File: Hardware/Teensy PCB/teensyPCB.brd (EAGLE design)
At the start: 100 x 50 mm, 4 parts, among them U1 HC_05

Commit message: updates
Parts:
- added TOBALANCE: (no value), SparkFun-Connectors:MOLEX-1X6_LOCK
- added U2: USD-SOCKETNEW, SparkFun-Connectors:MICRO-SD-SOCKET-PP
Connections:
- new net 5V: TOBALANCE.6
- new net ARDUINO_RX: TOBALANCE.3
- new net ARDUINO_TX: TOBALANCE.2
- new net ENABLE: TOBALANCE.1
- net 3.3V: now also TOBALANCE.5
- net GND: now also TOBALANCE.4; no longer U$1.10, U$1.11, U$1.12, U$1.13, U$1.14/A0, U$1.15/A1, U$1.18/A4, U$1.19/A5, U$1.22/A8, U$1.23/A9, U$1.7, U$1.9
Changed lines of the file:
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@@
 <layer number="54" name="bGND_GNDA" color="1" fill="9" visible="no" active="no"/>
 <layer number="56" name="wert" color="7" fill="1" visible="yes" active="yes"/>
+<layer number="57" name="tCAD" color="7" fill="1" visible="no" active="no"/>
 <layer number="90" name="Modules" color="5" fill="1" visible="no" active="no"/>
 <layer number="91" name="Nets" color="2" fill="1" visible="no" active="no"/>
@@
 <layer number="97" name="Info" color="7" fill="1" visible="no" active="no"/>
 <layer number="98" name="Guide" color="6" fill="1" visible="no" active="no"/>
+<layer number="99" name="SpiceOrder" color="7" fill="1" visible="no" active="no"/>
 <layer number="100" name="Muster" color="7" fill="1" visible="no" active="no"/>
 <layer number="101" name="Patch_Top" color="12" fill="4" visible="yes" active="yes"/>
@@
 <layer number="108" name="tplace-old" color="10" fill="1" visible="no" active="yes"/>
 <layer number="109" name="ref-old" color="11" fill="1" visible="no" active="yes"/>
+<layer number="110" name="fp0" color="7" fill="1" visible="yes" active="yes"/>
+<layer number="111" name="LPC17xx" color="7" fill="1" visible="yes" active="yes"/>
+<layer number="112" name="tSilk" color="7" fill="1" visible="yes" active="yes"/>
+<layer number="113" name="IDFDebug" color="4" fill="1" visible="yes" active="yes"/>
 <layer number="116" name="Patch_BOT" color="9" fill="4" visible="yes" active="yes"/>
 <layer number="121" name="_tsilk" color="7" fill="1" visible="yes" active="yes"/>
 <layer number="122" name="_bsilk" color="7" fill="1" visible="yes" active="yes"/>
+<layer number="123" name="tTestmark" color="7" fill="1" visible="yes" active="yes"/>
+<layer number="124" name="bTestmark" color="7" fill="1" visible="yes" active="yes"/>
 <layer number="125" name="_tNames" color="7" fill="1" visible="yes" active="yes"/>
+<layer number="126" name="_bNames" color="7" fill="1" visible="yes" active="yes"/>
+<layer number="127" name="_tValues" color="7" fill="1" visible="yes" active="yes"/>
+<layer number="128" name="_bValues" color="7" fill="1" visible="yes" active="yes"/>
+<layer number="131" name="tAdjust" color="7" fill="1" visible="yes" active="yes"/>
+<layer number="132" name="bAdjust" color="7" fill="1" visible="yes" active="yes"/>
 <layer number="144" name="Drill_legend" color="7" fill="1" visible="yes" active="yes"/>
+<layer number="150" name="Notes" color="7" fill="1" visible="yes" active="yes"/>
 <layer number="151" name="HeatSink" color="7" fill="1" visible="yes" active="yes"/>
+<layer number="152" name="_bDocu" color="7" fill="1" visible="yes" active="yes"/>
+<layer number="153" name="FabDoc1" color="7" fill="1" visible="yes" active="yes"/>
+<layer number="154" name="FabDoc2" color="7" fill="1" visible="yes" active="yes"/>
+<layer number="155" name="FabDoc3" color="7" fill="1" visible="yes" active="yes"/>
 <layer number="199" name="Contour" color="7" fill="1" visible="yes" active="yes"/>
 <layer number="200" name="200bmp" color="1" fill="10" visible="no" active="no"/>
@@
 <layer number="223" name="223bmp" color="24" fill="1" visible="no" active="no"/>
 <layer number="224" name="224bmp" color="25" fill="1" visible="no" active="no"/>
+<layer number="248" name="Housing" color="7" fill="1" visible="yes" active="yes"/>
+<layer number="249" name="Edge" color="7" fill="1" visible="yes" active="yes"/>
 <layer number="250" name="Descript" color="3" fill="1" visible="no" active="no"/>
 <layer number="251" name="SMDround" color="12" fill="11" visible="no" active="no"/>
@@
 <element name="J_BT_BOARD_1" library="Bluetooth_HC-05" package="BT_BOARD_FOOTPRINT" value="BLUETOOTH_BOARD" x="85" y="35"/>
 <element name="J_ULTRASONIC_1" library="HC-SR04" package="HC-SR04_FOOTPRINT" value="HC-SR04" x="10" y="35"/>
+<element name="U2" library="SparkFun-Connectors" package="MICRO-SD-SOCKET-PP" value="USD-SOCKETNEW" x="-60" y="5"/>
+<element name="TOBALANCE" library="SparkFun-Connectors" package="MOLEX-1X6_LOCK" value="" x="-70" y="-5"/>
 </elements>
 <signals>
@@
 <contactref element="U$1" pad="GND"/>
 <contactref element="U$1" pad="GND2"/>
-<contactref element="U$1" pad="18/A4"/>
-<contactref element="U$1" pad="19/A5"/>
-<contactref element="U$1" pad="11"/>
-<contactref element="U$1" pad="9"/>
-<contactref element="U$1" pad="23/A9"/>
-<contactref element="U$1" pad="22/A8"/>
-<contactref element="U$1" pad="13"/>
-<contactref element="U$1" pad="15/A1"/>
-<contactref element="U$1" pad="12"/>
-<contactref element="U$1" pad="14/A0"/>
-<contactref element="U$1" pad="7"/>
-<contactref element="U$1" pad="10"/>
-<wire x1="62.62" y1="31.35" x2="62.62" y2="33.89" width="0" layer="19" extent="1-1"/>
-<wire x1="62.62" y1="23.73" x2="62.62" y2="31.35" width="0" layer="19" extent="1-1"/>
-<wire x1="62.62" y1="21.19" x2="62.62" y2="23.73" width="0" layer="19" extent="1-1"/>
-<wire x1="55" y1="23.73" x2="62.62" y2="23.73" width="0" layer="19" extent="1-1"/>
-<wire x1="62.62" y1="13.57" x2="62.62" y2="21.19" width="0" layer="19" extent="1-1"/>
-<wire x1="62.62" y1="11.03" x2="62.62" y2="13.57" width="0" layer="19" extent="1-1"/>
-<wire x1="62.62" y1="8.49" x2="62.62" y2="11.03" width="0" layer="19" extent="1-1"/>
-<wire x1="55" y1="8.49" x2="62.62" y2="8.49" width="0" layer="19" extent="1-1"/>
-<wire x1="47.38" y1="8.49" x2="55" y2="8.49" width="0" layer="19" extent="1-1"/>
-<wire x1="47.38" y1="11.03" x2="47.38" y2="8.49" width="0" layer="19" extent="1-1"/>
-<wire x1="47.38" y1="13.57" x2="47.38" y2="11.03" width="0" layer="19" extent="1-1"/>
-<wire x1="47.38" y1="16.11" x2="47.38" y2="13.57" width="0" layer="19" extent="1-1"/>
-<wire x1="47.38" y1="21.19" x2="47.38" y2="16.11" width="0" layer="19" extent="1-1"/>
-<wire x1="47.38" y1="41.51" x2="62.62" y2="33.89" width="0" layer="19" extent="1-1"/>
+<contactref element="TOBALANCE" pad="4"/>
+<wire x1="55" y1="23.73" x2="47.38" y2="41.51" width="0" layer="19" extent="1-1"/>
+<wire x1="55" y1="8.49" x2="55" y2="23.73" width="0" layer="19" extent="1-1"/>
+<wire x1="-62.38" y1="-5.254" x2="55" y2="8.49" width="0" layer="19" extent="1-1"/>
 </signal>
 <signal name="VIN">
@@
 <contactref element="U$1" pad="3.3V1"/>
 <contactref element="U$1" pad="3.3V"/>
+<contactref element="TOBALANCE" pad="5"/>
 <wire x1="57.54" y1="23.73" x2="62.62" y2="36.43" width="0" layer="19" extent="1-1"/>
 <wire x1="52.46" y1="8.49" x2="57.54" y2="23.73" width="0" layer="19" extent="1-1"/>
+<wire x1="-59.84" y1="-5" x2="52.46" y2="8.49" width="0" layer="19" extent="1-1"/>
 </signal>
 <signal name="VBAT">
@@
 <contactref element="U$1" pad="VUSB"/>
 </signal>
+<signal name="5V">
+<contactref element="TOBALANCE" pad="6"/>
+</signal>
+<signal name="ARDUINO_RX">
+<contactref element="TOBALANCE" pad="3"/>
+</signal>
+<signal name="ARDUINO_TX">
+<contactref element="TOBALANCE" pad="2"/>
+</signal>
+<signal name="ENABLE">
+<contactref element="TOBALANCE" pad="1"/>
+</signal>
 </signals>

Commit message: Jeysen connected SD card in eagle schematic
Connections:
- new net CS: U$1.10, U2.2
- new net MISO: U$1.12, U2.7
- new net MOSI: U$1.11, U2.3
- new net SCK: U$1.13, U2.5
- net 3.3V: now also U2.4
- net GND: now also U2.6
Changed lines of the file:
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@@
 <?xml version="1.0" encoding="utf-8"?>
 <!DOCTYPE eagle SYSTEM "eagle.dtd">
-<eagle version="7.2.0">
+<eagle version="7.5.0">
 <drawing>
 <settings>
@@
 <contactref element="U$1" pad="GND2"/>
 <contactref element="TOBALANCE" pad="4"/>
+<contactref element="U2" pad="6"/>
 <wire x1="55" y1="23.73" x2="47.38" y2="41.51" width="0" layer="19" extent="1-1"/>
 <wire x1="55" y1="8.49" x2="55" y2="23.73" width="0" layer="19" extent="1-1"/>
-<wire x1="-62.38" y1="-5.254" x2="55" y2="8.49" width="0" layer="19" extent="1-1"/>
+<wire x1="-63.44" y1="15.9" x2="47.38" y2="41.51" width="0" layer="19" extent="1-1"/>
+<wire x1="-62.38" y1="-5.254" x2="-63.44" y2="15.9" width="0" layer="19" extent="1-1"/>
 </signal>
 <signal name="VIN">
@@
 <contactref element="U$1" pad="3.3V"/>
 <contactref element="TOBALANCE" pad="5"/>
+<contactref element="U2" pad="4"/>
 <wire x1="57.54" y1="23.73" x2="62.62" y2="36.43" width="0" layer="19" extent="1-1"/>
 <wire x1="52.46" y1="8.49" x2="57.54" y2="23.73" width="0" layer="19" extent="1-1"/>
 <wire x1="-59.84" y1="-5" x2="52.46" y2="8.49" width="0" layer="19" extent="1-1"/>
+<wire x1="-65.64" y1="15.9" x2="-59.84" y2="-5" width="0" layer="19" extent="1-1"/>
 </signal>
 <signal name="VBAT">
@@
 <contactref element="TOBALANCE" pad="1"/>
 </signal>
+<signal name="SCK">
+<contactref element="U2" pad="5"/>
+<contactref element="U$1" pad="13"/>
+<wire x1="-64.54" y1="15.7" x2="62.62" y2="8.49" width="0" layer="19" extent="1-1"/>
+</signal>
+<signal name="MISO">
+<contactref element="U2" pad="7"/>
+<contactref element="U$1" pad="12"/>
+<wire x1="-62.34" y1="15.7" x2="47.38" y2="8.49" width="0" layer="19" extent="1-1"/>
+</signal>
+<signal name="MOSI">
+<contactref element="U2" pad="3"/>
+<contactref element="U$1" pad="11"/>
+<wire x1="-66.74" y1="15.7" x2="47.38" y2="11.03" width="0" layer="19" extent="1-1"/>
+</signal>
+<signal name="CS">
+<contactref element="U$1" pad="10"/>
+<contactref element="U2" pad="2"/>
+<wire x1="-67.84" y1="15.3" x2="47.38" y2="13.57" width="0" layer="19" extent="1-1"/>
+</signal>
 </signals>

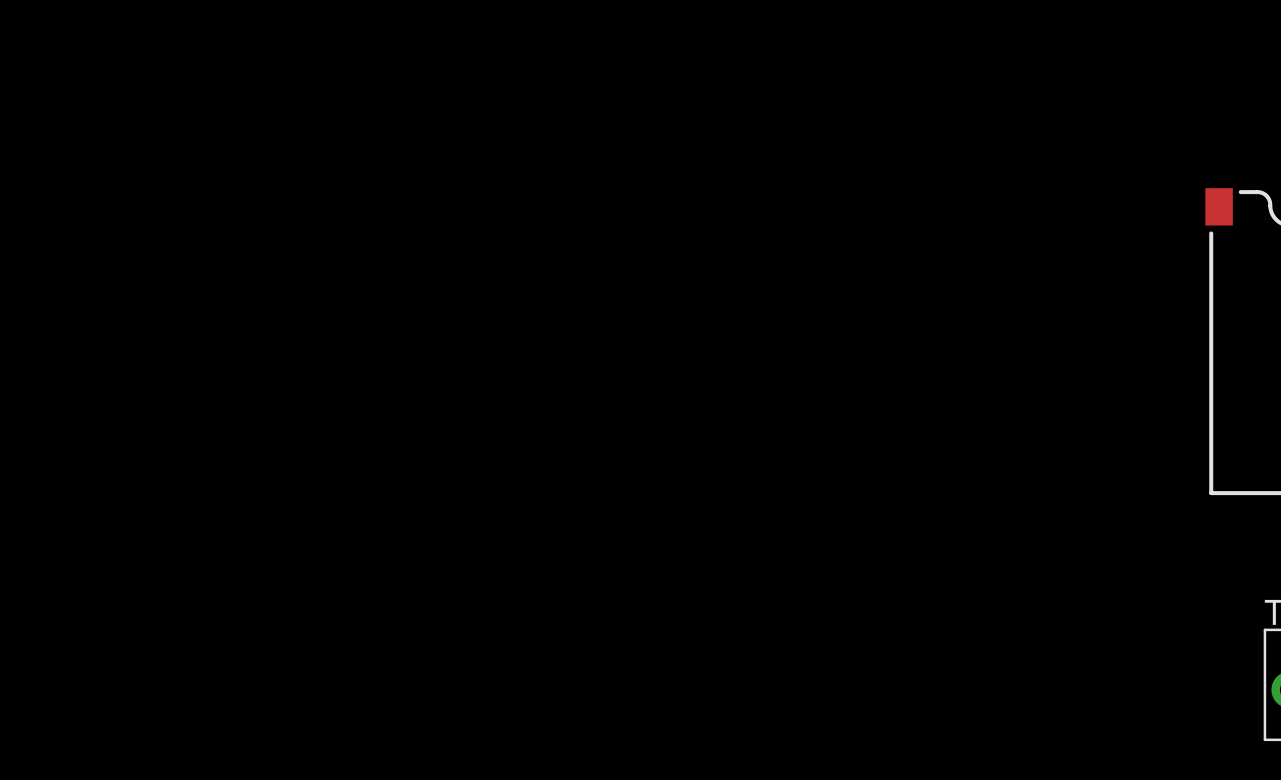
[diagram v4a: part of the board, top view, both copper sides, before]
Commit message: Updated OLED module library and added modules to teensy PCB
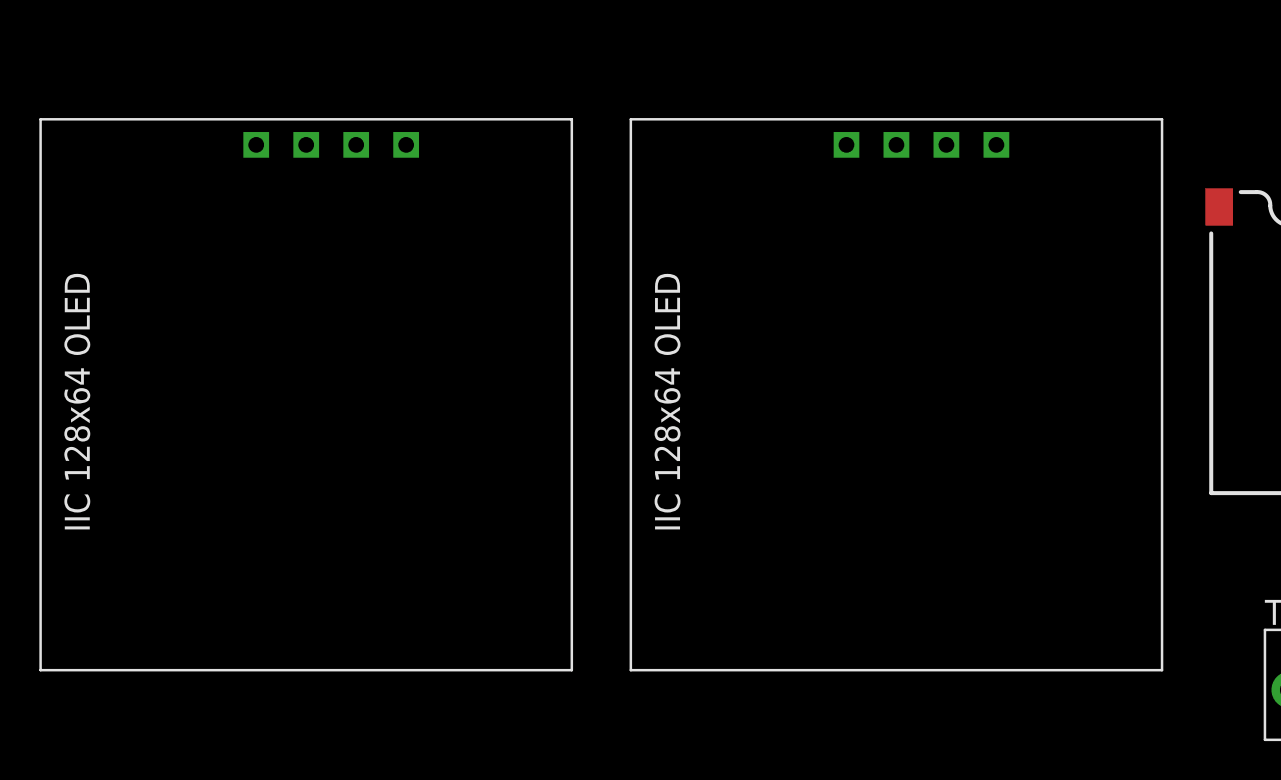
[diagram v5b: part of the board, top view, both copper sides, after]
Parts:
- added U$2, U$3: IIC128X64OLED, IIC OLED MODULE LIBRARY:IIC128X64OLED
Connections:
- new net SCL0: U$1.19/A5, U$2.SCL
- new net SCL1: U$1.29, U$3.SCL
- new net SDA0: U$1.18/A4, U$2.SDA
- new net SDA1: U$1.30, U$3.SDA
- net 3.3V: now also U$2.VCC, U$3.VCC
- net GND: now also U$2.GND, U$3.GND
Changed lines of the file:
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@@
 <?xml version="1.0" encoding="utf-8"?>
 <!DOCTYPE eagle SYSTEM "eagle.dtd">
-<eagle version="7.5.0">
+<eagle version="7.2.0">
 <drawing>
 <settings>
@@
 <element name="U2" library="SparkFun-Connectors" package="MICRO-SD-SOCKET-PP" value="USD-SOCKETNEW" x="-60" y="5"/>
 <element name="TOBALANCE" library="SparkFun-Connectors" package="MOLEX-1X6_LOCK" value="" x="-70" y="-5"/>
+<element name="U$2" library="IIC OLED MODULE LIBRARY" package="IIC128X64OLED" value="IIC128X64OLED" x="-90" y="10"/>
+<element name="U$3" library="IIC OLED MODULE LIBRARY" package="IIC128X64OLED" value="IIC128X64OLED" x="-120" y="10"/>
 </elements>
 <signals>
@@
 <contactref element="TOBALANCE" pad="4"/>
 <contactref element="U2" pad="6"/>
+<contactref element="U$2" pad="GND"/>
+<contactref element="U$3" pad="GND"/>
+<wire x1="-84.92" y1="22.7" x2="-114.92" y2="22.7" width="0" layer="19" extent="1-1"/>
+<wire x1="-63.44" y1="15.9" x2="-84.92" y2="22.7" width="0" layer="19" extent="1-1"/>
+<wire x1="-62.38" y1="-5.254" x2="-63.44" y2="15.9" width="0" layer="19" extent="1-1"/>
+<wire x1="47.38" y1="41.51" x2="-63.44" y2="15.9" width="0" layer="19" extent="1-1"/>
 <wire x1="55" y1="23.73" x2="47.38" y2="41.51" width="0" layer="19" extent="1-1"/>
 <wire x1="55" y1="8.49" x2="55" y2="23.73" width="0" layer="19" extent="1-1"/>
-<wire x1="-63.44" y1="15.9" x2="47.38" y2="41.51" width="0" layer="19" extent="1-1"/>
-<wire x1="-62.38" y1="-5.254" x2="-63.44" y2="15.9" width="0" layer="19" extent="1-1"/>
 </signal>
 <signal name="VIN">
@@
 <contactref element="TOBALANCE" pad="5"/>
 <contactref element="U2" pad="4"/>
-<wire x1="57.54" y1="23.73" x2="62.62" y2="36.43" width="0" layer="19" extent="1-1"/>
-<wire x1="52.46" y1="8.49" x2="57.54" y2="23.73" width="0" layer="19" extent="1-1"/>
-<wire x1="-59.84" y1="-5" x2="52.46" y2="8.49" width="0" layer="19" extent="1-1"/>
-<wire x1="-65.64" y1="15.9" x2="-59.84" y2="-5" width="0" layer="19" extent="1-1"/>
+<contactref element="U$2" pad="VCC"/>
+<contactref element="U$3" pad="VCC"/>
+<wire x1="-92.54" y1="22.7" x2="-122.54" y2="22.7" width="0" layer="19" extent="1-1"/>
+<wire x1="-65.64" y1="15.9" x2="-92.54" y2="22.7" width="0" layer="19" extent="1-1"/>
+<wire x1="-59.84" y1="-5" x2="-65.64" y2="15.9" width="0" layer="19" extent="1-1"/>
+<wire x1="52.46" y1="8.49" x2="-59.84" y2="-5" width="0" layer="19" extent="1-1"/>
+<wire x1="57.54" y1="23.73" x2="52.46" y2="8.49" width="0" layer="19" extent="1-1"/>
+<wire x1="62.62" y1="36.43" x2="57.54" y2="23.73" width="0" layer="19" extent="1-1"/>
 </signal>
 <signal name="VBAT">
@@
 <wire x1="-67.84" y1="15.3" x2="47.38" y2="13.57" width="0" layer="19" extent="1-1"/>
 </signal>
+<signal name="SDA0">
+<contactref element="U$1" pad="18/A4"/>
+<contactref element="U$2" pad="SDA"/>
+<wire x1="-87.46" y1="22.7" x2="62.62" y2="21.19" width="0" layer="19" extent="1-1"/>
+</signal>
+<signal name="SCL0">
+<contactref element="U$1" pad="19/A5"/>
+<contactref element="U$2" pad="SCL"/>
+<wire x1="-90" y1="22.7" x2="62.62" y2="23.73" width="0" layer="19" extent="1-1"/>
+</signal>
+<signal name="SDA1">
+<contactref element="U$1" pad="30"/>
+<contactref element="U$3" pad="SDA"/>
+<wire x1="57.54" y1="13.57" x2="-117.46" y2="22.7" width="0" layer="19" extent="1-1"/>
+</signal>
+<signal name="SCL1">
+<contactref element="U$1" pad="29"/>
+<contactref element="U$3" pad="SCL"/>
+<wire x1="57.54" y1="11.03" x2="-120" y2="22.7" width="0" layer="19" extent="1-1"/>
+</signal>
 </signals>

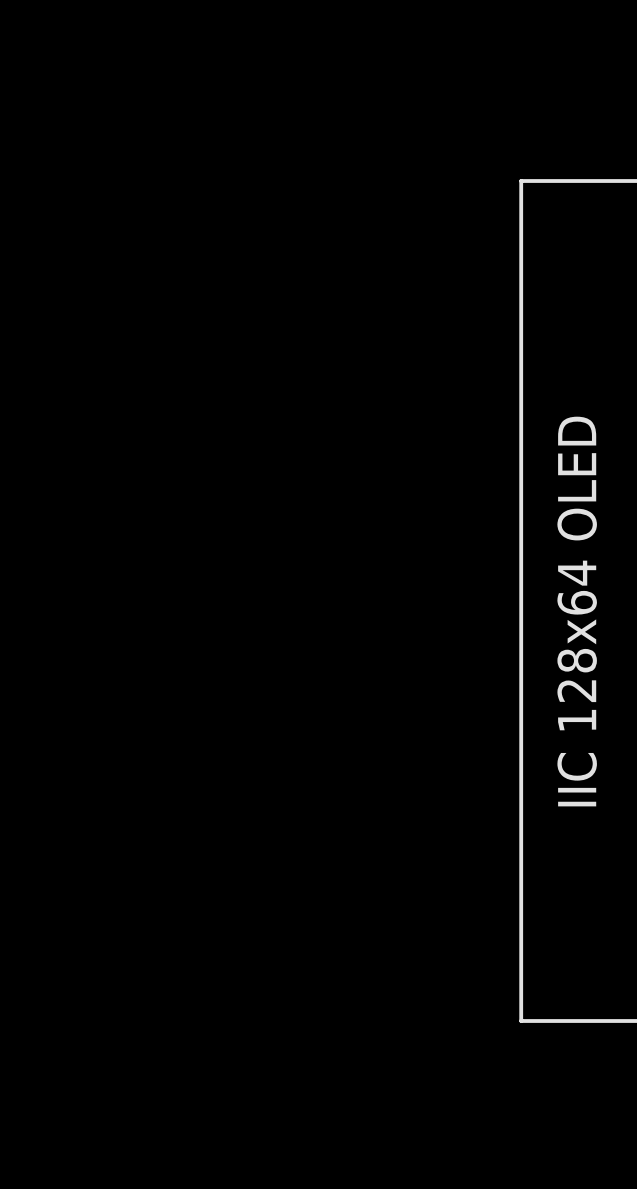
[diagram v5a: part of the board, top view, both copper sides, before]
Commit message: Added audio amp to pcb
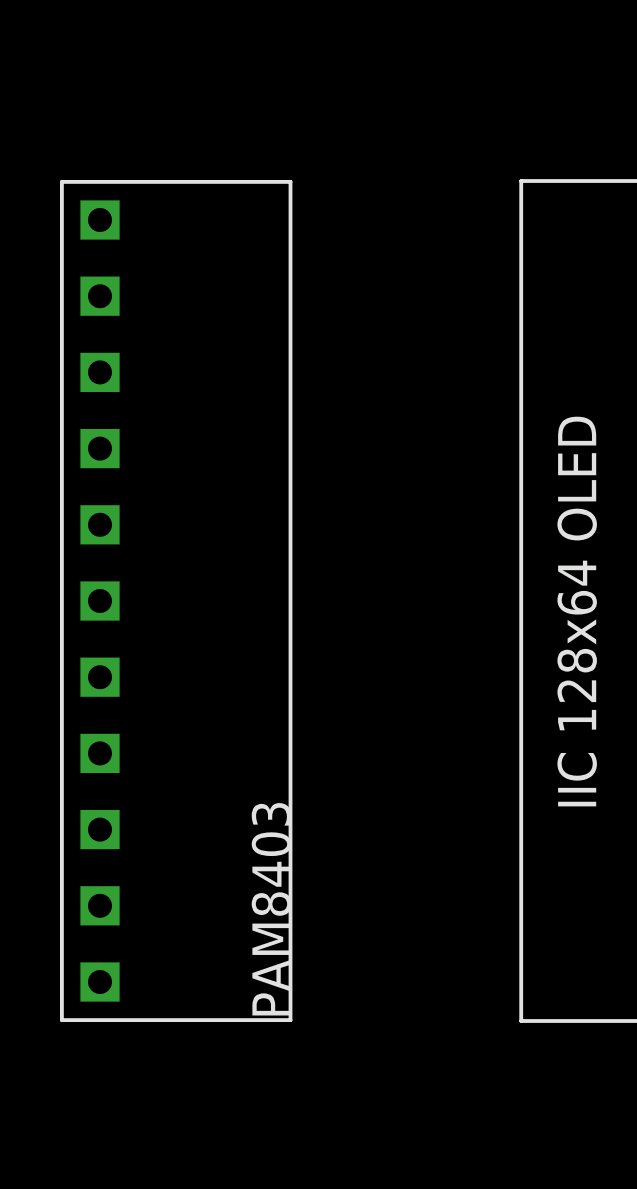
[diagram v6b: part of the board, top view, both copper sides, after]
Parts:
- added U$4: AUDIOAMP, CLASS D AUDIO AMP:AUDIOAMP
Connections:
- net 5V: now also U$4.+5V
- net GND: now also U$4.GND0, U$4.GND1, U$4.GND2
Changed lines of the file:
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@@
 <element name="U$2" library="IIC OLED MODULE LIBRARY" package="IIC128X64OLED" value="IIC128X64OLED" x="-90" y="10"/>
 <element name="U$3" library="IIC OLED MODULE LIBRARY" package="IIC128X64OLED" value="IIC128X64OLED" x="-120" y="10"/>
+<element name="U$4" library="CLASS D AUDIO AMP" package="AUDIOAMP" value="AUDIOAMP" x="-145" y="10"/>
 </elements>
 <signals>
@@
 <contactref element="U$2" pad="GND"/>
 <contactref element="U$3" pad="GND"/>
+<contactref element="U$4" pad="GND0"/>
+<contactref element="U$4" pad="GND1"/>
+<contactref element="U$4" pad="GND2"/>
+<wire x1="-147.54" y1="4.92" x2="-147.54" y2="-0.16" width="0" layer="19" extent="1-1"/>
+<wire x1="-147.54" y1="12.54" x2="-147.54" y2="4.92" width="0" layer="19" extent="1-1"/>
+<wire x1="-114.92" y1="22.7" x2="-147.54" y2="12.54" width="0" layer="19" extent="1-1"/>
 <wire x1="-84.92" y1="22.7" x2="-114.92" y2="22.7" width="0" layer="19" extent="1-1"/>
 <wire x1="-63.44" y1="15.9" x2="-84.92" y2="22.7" width="0" layer="19" extent="1-1"/>
@@
 <signal name="5V">
 <contactref element="TOBALANCE" pad="6"/>
+<contactref element="U$4" pad="+5V"/>
+<wire x1="-57.3" y1="-5.254" x2="-147.54" y2="10" width="0" layer="19" extent="1-1"/>
 </signal>
 <signal name="ARDUINO_RX">
